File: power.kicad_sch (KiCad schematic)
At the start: 40 parts, among them T1 net-tie, U2 TPS546D24ARVFR

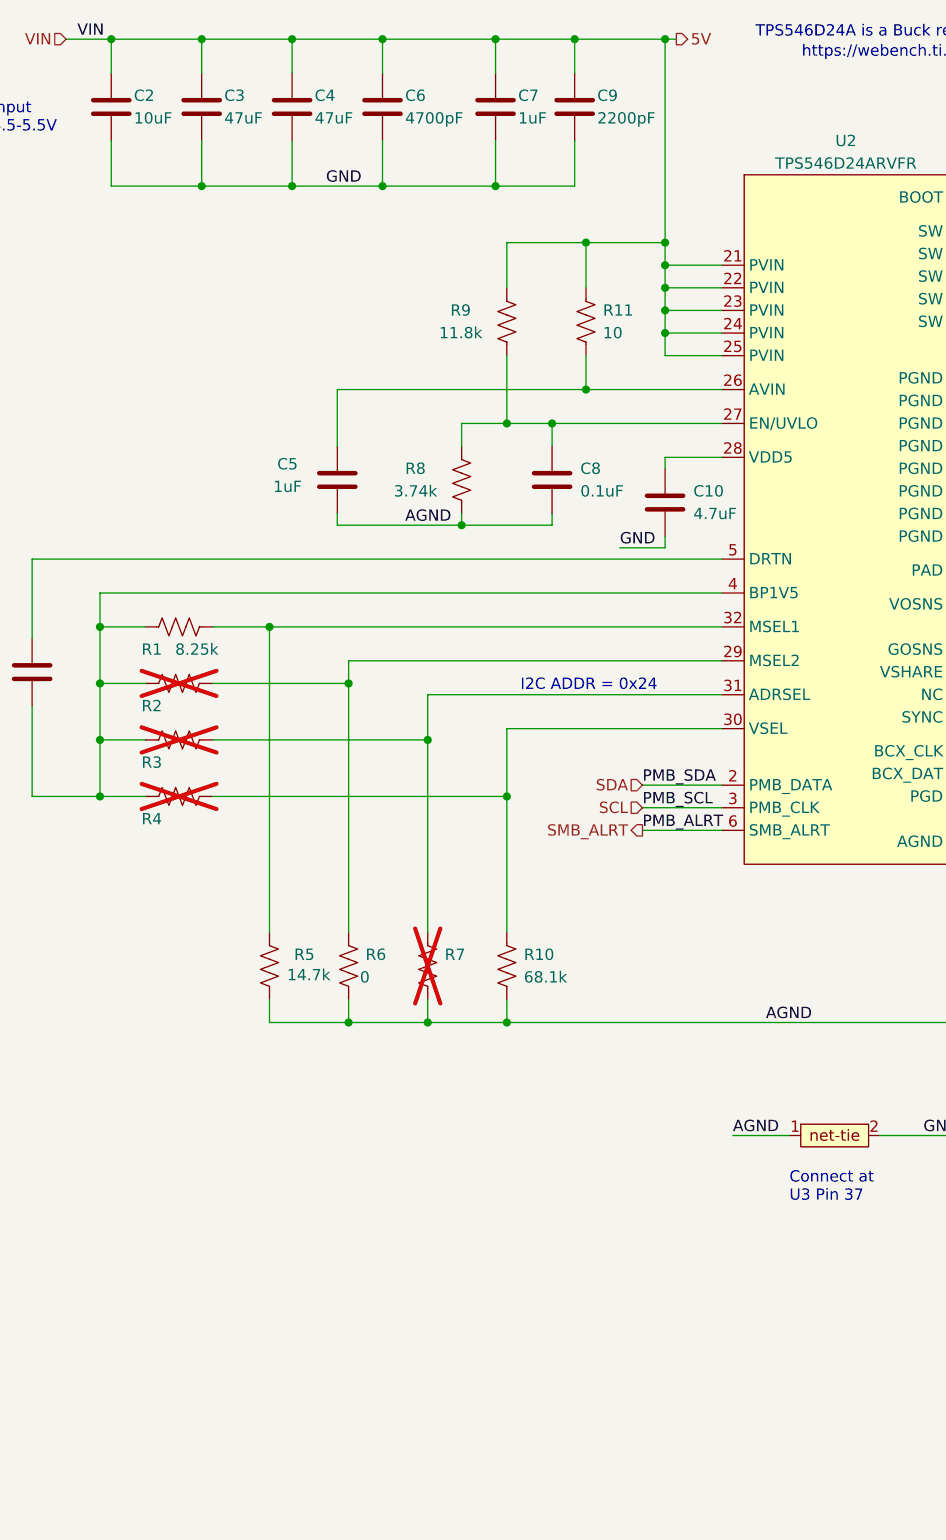
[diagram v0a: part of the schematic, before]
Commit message: add tps82130 for wide-VIN support
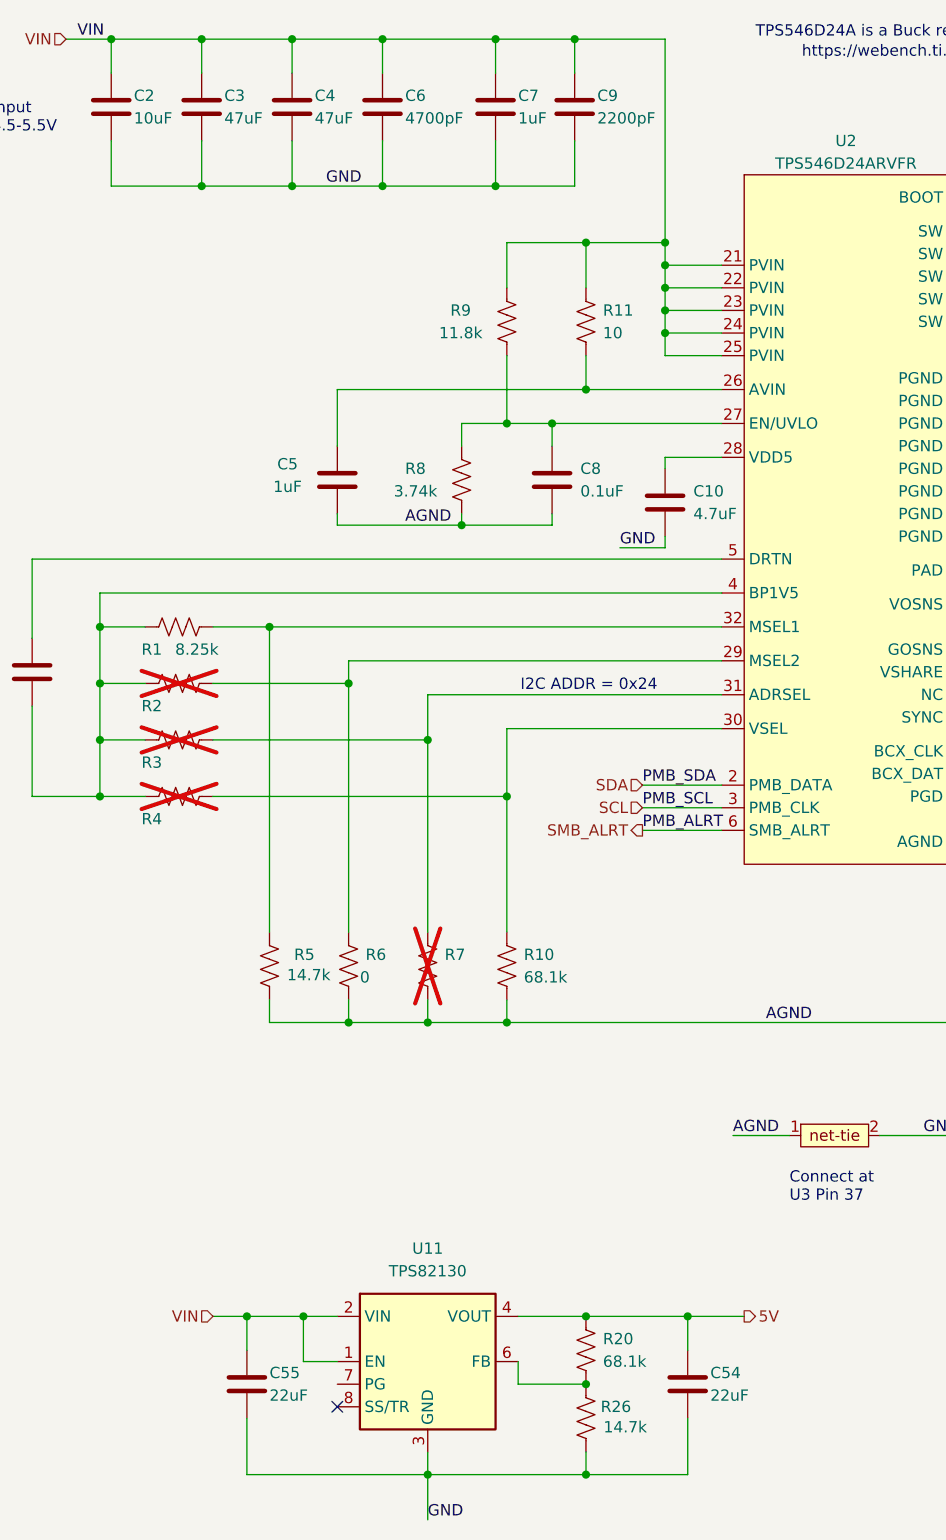
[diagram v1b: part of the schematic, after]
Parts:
- added C54, C55: 22uF, Capacitor_SMD:C_0805_2012Metric, symbol Device:C
- added R20: 68.1k, Resistor_SMD:R_0402_1005Metric, symbol Device:R_US
- added R26: 14.7k, Resistor_SMD:R_0402_1005Metric, symbol Device:R_US
- added U11: TPS82130, Package_LGA:Texas_SIL0008D_MicroSiP-8-1EP_2.8x3mm_P0.65mm_EP1.1x1.9mm_ThermalVias, symbol Regulator_Switching:TPS82130
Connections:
- net 5V: now also C54.1, R20.1, U11.4 (VOUT), U11.5 (VOUT); no longer C2.1, C3.1, C4.1, C6.1, C7.1, C9.1, R11.1, R9.1, U2.21 (PVIN), U2.22 (PVIN), U2.23 (PVIN), U2.24 (PVIN), U2.25 (PVIN)
- net GND: now also C54.2, C55.2, R26.1, U11.3 (GND), U11.9 (GND)
- new net: R20.2, R26.2, U11.6 (FB)
- new net VIN: C2.1, C3.1, C4.1, C55.1, C6.1, C7.1, C9.1, R11.1, R9.1, U11.1 (EN), U11.2 (VIN), U2.21 (PVIN), U2.22 (PVIN), U2.23 (PVIN), U2.24 (PVIN), U2.25 (PVIN)
- no-connect marks 5 -> 6

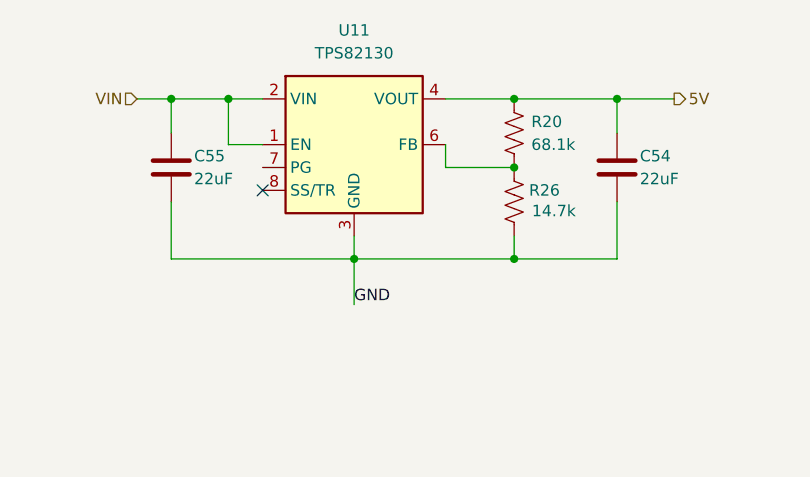
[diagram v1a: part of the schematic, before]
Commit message: add 0805 0R fallback jumper from VIN->5V
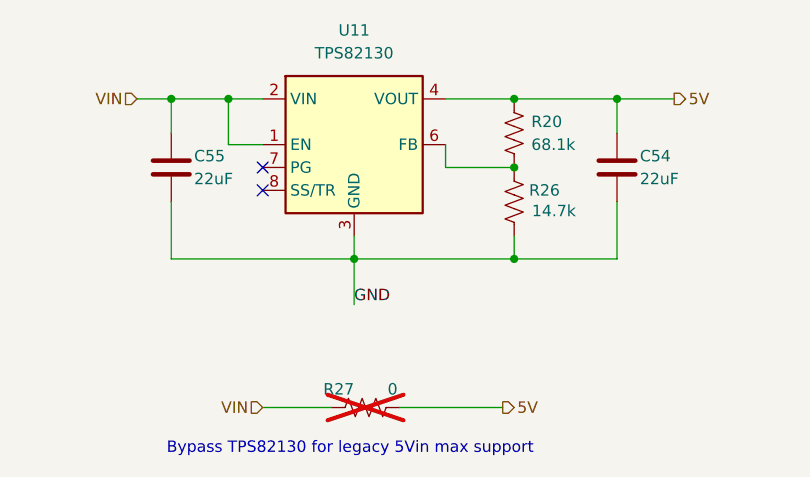
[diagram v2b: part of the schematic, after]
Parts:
- added R27: 0, Resistor_SMD:R_0805_2012Metric, symbol Device:R_US
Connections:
- net 5V: now also R27.2
- net VIN: now also R27.1
- no-connect marks 6 -> 7
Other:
- note added: "Bypass TPS82130 for legacy 5Vin max support"
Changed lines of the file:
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@@
 		)
 	)
+	(text "Bypass TPS82130 for legacy 5Vin max support"
+		(exclude_from_sim no)
+		(at 54.102 200.914 0)
+		(effects
+			(font
+				(size 1.27 1.27)
+			)
+			(justify left bottom)
+		)
+	)
 	(text "I2C ADDR = 0x24"
 		(exclude_from_sim no)
@@
 	)
 	(no_connect
+		(at 64.77 168.91)
+	)
+	(no_connect
 		(at 135.89 93.98)
 	)
@@
 	(wire
 		(pts
+			(xy 80.01 195.58) (xy 91.44 195.58)
+		)
+		(stroke
+			(width 0)
+			(type default)
+		)
+	)
+	(wire
+		(pts
 			(xy 101.6 45.72) (xy 107.95 45.72)
 		)
@@
 	(wire
 		(pts
+			(xy 64.77 195.58) (xy 72.39 195.58)
+		)
+		(stroke
+			(width 0)
+			(type default)
+		)
+	)
+	(wire
+		(pts
 			(xy 54.61 161.29) (xy 54.61 165.1)
 		)
@@
 		)
 	)
+	(hierarchical_label "VIN"
+		(shape input)
+		(at 64.77 195.58 180)
+		(effects
+			(font
+				(size 1.27 1.27)
+			)
+			(justify right)
+		)
+	)
 	(hierarchical_label "PGOOD"
 		(shape output)
@@
 		)
 	)
+	(hierarchical_label "5V"
+		(shape output)
+		(at 91.44 195.58 0)
+		(effects
+			(font
+				(size 1.27 1.27)
+			)
+			(justify left)
+		)
+	)
 	(hierarchical_label "VIN"
 		(shape input)
@@
 					(unit 1)
 				)
+			)
+		)
+	)
+	(symbol
+		(lib_id "Device:R_US")
+		(at 76.2 195.58 90)
+		(unit 1)
+		(exclude_from_sim no)
+		(in_bom yes)
+		(on_board yes)
+		(dnp yes)
+		(property "Reference" "R27"
+			(at 74.93 193.548 90)
+			(effects
+				(font
+					(size 1.27 1.27)
+				)
+				(justify left)
+			)
+		)
+		(property "Value" "0"
+			(at 79.756 193.548 90)
+			(effects
+				(font
+					(size 1.27 1.27)
+				)
+				(justify left)
+			)
+		)
+		(property "Footprint" "Resistor_SMD:R_0805_2012Metric"
+			(at 76.454 194.564 90)
+			(effects
+				(font
+					(size 1.27 1.27)
+				)
+				(hide yes)
+			)
+		)
+		(property "Datasheet" "~"
+			(at 76.2 195.58 0)
+			(effects
+				(font
+					(size 1.27 1.27)
+				)
+				(hide yes)
+			)
+		)
+		(property "Description" ""
+			(at 76.2 195.58 0)
+			(effects
+				(font
+					(size 1.27 1.27)
+				)
+				(hide yes)
+			)
+		)
+		(property "DK" "YAG1327DKR-ND"
+			(at 76.2 195.58 0)
+			(effects
+				(font
+					(size 1.27 1.27)
+				)
+				(hide yes)
+			)
+		)
+		(property "PARTNO" "RC0805JR-070RP"
+			(at 76.2 195.58 0)
+			(effects
+				(font
+					(size 1.27 1.27)
+				)
+				(hide yes)
+			)
+		)
+		(pin "1"
+		)
+		(pin "2"
+		)
+		(instances
+			(project "bitaxeGamma"
+				(path "/e63e39d7-6ac0-4ffd-8aa3-1841a4541b55/8ec0a9c6-2b78-44ef-a83d-9047d2828409"
+					(reference "R27")
+					(unit 1)
+				)

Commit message: fork sil0008d footprint to fix pad sizes
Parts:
- U11: footprint Package_LGA:Texas_SIL0008D_MicroSiP-8-1EP_2.8x3mm_P0.65mm_EP1.1x1.9mm_ThermalVias -> bitaxe:Texas_SIL0008D_MicroSiP-8-1EP_2.8x3mm_P0.65mm_EP1.1x1.9mm_ThermalVias
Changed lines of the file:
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@@
 			)
 		)
-		(property "Footprint" "Package_LGA:Texas_SIL0008D_MicroSiP-8-1EP_2.8x3mm_P0.65mm_EP1.1x1.9mm_ThermalVias"
+		(property "Footprint" "bitaxe:Texas_SIL0008D_MicroSiP-8-1EP_2.8x3mm_P0.65mm_EP1.1x1.9mm_ThermalVias"
 			(at 74.93 182.88 0)
 			(effects
